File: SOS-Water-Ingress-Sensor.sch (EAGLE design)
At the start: 12 parts

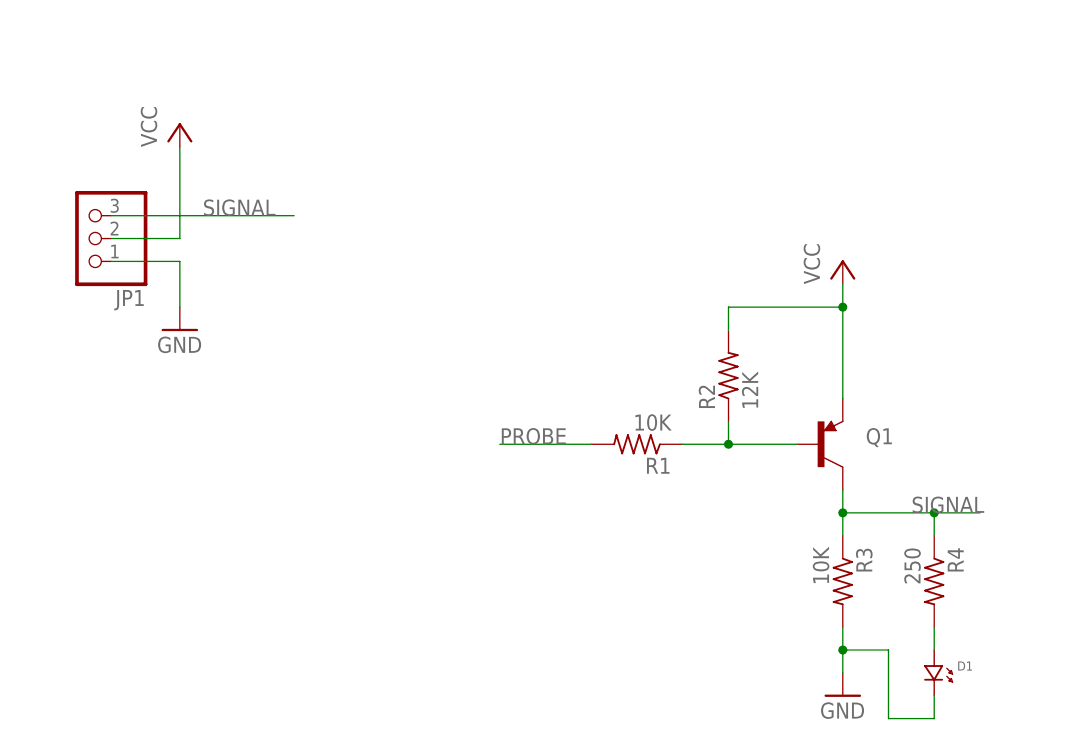
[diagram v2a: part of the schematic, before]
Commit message: Update silkscreen and layout.
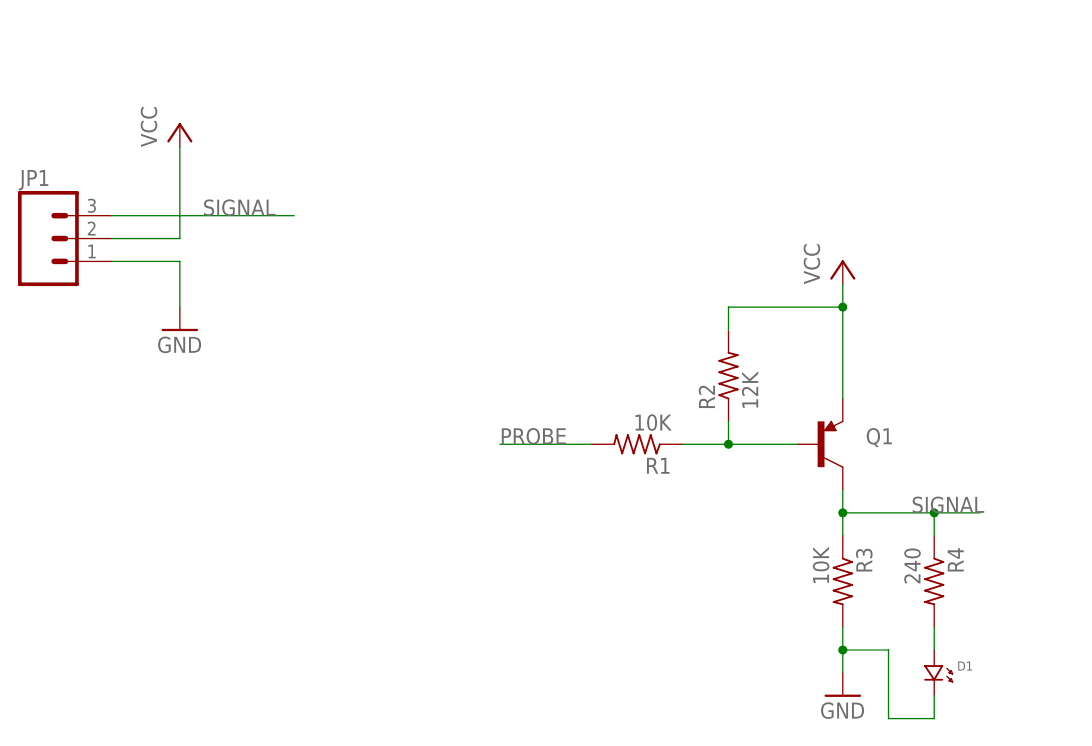
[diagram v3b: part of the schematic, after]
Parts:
- JP1: device pinhead+:PINHD-1X3 -> SparkFun-Connectors:M03PTH
- R4: value 250 -> 240
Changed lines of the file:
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@@
 <?xml version="1.0" encoding="utf-8"?>
 <!DOCTYPE eagle SYSTEM "eagle.dtd">
-<eagle version="7.6.0">
+<eagle version="7.4.0">
 <drawing>
 <settings>
@@
 <grid distance="0.1" unitdist="inch" unit="inch" style="lines" multiple="1" display="no" altdistance="0.01" altunitdist="inch" altunit="inch"/>
 <layers>
-<layer number="1" name="Top" color="4" fill="1" visible="no" active="no"/>
-<layer number="2" name="Route2" color="1" fill="3" visible="no" active="no"/>
-<layer number="3" name="Route3" color="4" fill="3" visible="no" active="no"/>
-<layer number="14" name="Route14" color="1" fill="6" visible="no" active="no"/>
-<layer number="15" name="Route15" color="4" fill="6" visible="no" active="no"/>
-<layer number="16" name="Bottom" color="1" fill="1" visible="no" active="no"/>
-<layer number="17" name="Pads" color="2" fill="1" visible="no" active="no"/>
-<layer number="18" name="Vias" color="2" fill="1" visible="no" active="no"/>
-<layer number="19" name="Unrouted" color="6" fill="1" visible="no" active="no"/>
-<layer number="20" name="Dimension" color="15" fill="1" visible="no" active="no"/>
-<layer number="21" name="tPlace" color="7" fill="1" visible="no" active="no"/>
-<layer number="22" name="bPlace" color="7" fill="1" visible="no" active="no"/>
-<layer number="23" name="tOrigins" color="15" fill="1" visible="no" active="no"/>
-<layer number="24" name="bOrigins" color="15" fill="1" visible="no" active="no"/>
-<layer number="25" name="tNames" color="7" fill="1" visible="no" active="no"/>
-<layer number="26" name="bNames" color="7" fill="1" visible="no" active="no"/>
-<layer number="27" name="tValues" color="7" fill="1" visible="no" active="no"/>
-<layer number="28" name="bValues" color="7" fill="1" visible="no" active="no"/>
+<layer number="1" name="Top" color="4" fill="1" visible="yes" active="no"/>
+<layer number="2" name="Route2" color="1" fill="3" visible="yes" active="no"/>
+<layer number="3" name="Route3" color="4" fill="3" visible="yes" active="no"/>
+<layer number="14" name="Route14" color="1" fill="6" visible="yes" active="no"/>
+<layer number="15" name="Route15" color="4" fill="6" visible="yes" active="no"/>
+<layer number="16" name="Bottom" color="1" fill="1" visible="yes" active="no"/>
+<layer number="17" name="Pads" color="2" fill="1" visible="yes" active="no"/>
+<layer number="18" name="Vias" color="2" fill="1" visible="yes" active="no"/>
+<layer number="19" name="Unrouted" color="6" fill="1" visible="yes" active="no"/>
+<layer number="20" name="Dimension" color="15" fill="1" visible="yes" active="no"/>
+<layer number="21" name="tPlace" color="7" fill="1" visible="yes" active="no"/>
+<layer number="22" name="bPlace" color="7" fill="1" visible="yes" active="no"/>
+<layer number="23" name="tOrigins" color="15" fill="1" visible="yes" active="no"/>
+<layer number="24" name="bOrigins" color="15" fill="1" visible="yes" active="no"/>
+<layer number="25" name="tNames" color="7" fill="1" visible="yes" active="no"/>
+<layer number="26" name="bNames" color="7" fill="1" visible="yes" active="no"/>
+<layer number="27" name="tValues" color="7" fill="1" visible="yes" active="no"/>
+<layer number="28" name="bValues" color="7" fill="1" visible="yes" active="no"/>
 <layer number="29" name="tStop" color="7" fill="3" visible="no" active="no"/>
 <layer number="30" name="bStop" color="7" fill="6" visible="no" active="no"/>
@@
 <layer number="35" name="tGlue" color="7" fill="4" visible="no" active="no"/>
 <layer number="36" name="bGlue" color="7" fill="5" visible="no" active="no"/>
-<layer number="37" name="tTest" color="7" fill="1" visible="no" active="no"/>
-<layer number="38" name="bTest" color="7" fill="1" visible="no" active="no"/>
+<layer number="37" name="tTest" color="7" fill="1" visible="yes" active="no"/>
+<layer number="38" name="bTest" color="7" fill="1" visible="yes" active="no"/>
 <layer number="39" name="tKeepout" color="4" fill="11" visible="no" active="no"/>
 <layer number="40" name="bKeepout" color="1" fill="11" visible="no" active="no"/>
@@
 <layer number="44" name="Drills" color="7" fill="1" visible="no" active="no"/>
 <layer number="45" name="Holes" color="7" fill="1" visible="no" active="no"/>
-<layer number="46" name="Milling" color="3" fill="1" visible="no" active="no"/>
-<layer number="47" name="Measures" color="7" fill="1" visible="no" active="no"/>
-<layer number="48" name="Document" color="7" fill="1" visible="no" active="no"/>
-<layer number="49" name="Reference" color="7" fill="1" visible="no" active="no"/>
-<layer number="50" name="dxf" color="7" fill="1" visible="no" active="no"/>
-<layer number="51" name="tDocu" color="7" fill="1" visible="no" active="no"/>
-<layer number="52" name="bDocu" color="7" fill="1" visible="no" active="no"/>
-<layer number="53" name="tGND_GNDA" color="7" fill="9" visible="no" active="no"/>
-<layer number="54" name="bGND_GNDA" color="1" fill="9" visible="no" active="no"/>
-<layer number="56" name="wert" color="7" fill="1" visible="no" active="no"/>
-<layer number="57" name="tCAD" color="7" fill="1" visible="no" active="no"/>
-<layer number="59" name="tCarbon" color="7" fill="1" visible="no" active="no"/>
-<layer number="60" name="bCarbon" color="7" fill="1" visible="no" active="no"/>
+<layer number="46" name="Milling" color="3" fill="1" visible="yes" active="no"/>
+<layer number="47" name="Measures" color="7" fill="1" visible="yes" active="no"/>
+<layer number="48" name="Document" color="7" fill="1" visible="yes" active="no"/>
+<layer number="49" name="Reference" color="7" fill="1" visible="yes" active="no"/>
+<layer number="50" name="dxf" color="7" fill="1" visible="yes" active="no"/>
+<layer number="51" name="tDocu" color="7" fill="1" visible="yes" active="no"/>
+<layer number="52" name="bDocu" color="7" fill="1" visible="yes" active="no"/>
+<layer number="53" name="tGND_GNDA" color="7" fill="9" visible="yes" active="no"/>
+<layer number="54" name="bGND_GNDA" color="1" fill="9" visible="yes" active="no"/>
+<layer number="56" name="wert" color="7" fill="1" visible="yes" active="no"/>
+<layer number="57" name="tCAD" color="7" fill="1" visible="yes" active="no"/>
+<layer number="59" name="tCarbon" color="7" fill="1" visible="yes" active="no"/>
+<layer number="60" name="bCarbon" color="7" fill="1" visible="yes" active="no"/>
 <layer number="90" name="Modules" color="5" fill="1" visible="yes" active="yes"/>
 <layer number="91" name="Nets" color="2" fill="1" visible="yes" active="yes"/>
@@
 <part name="U$2" library="BlueRobotics-JST-GH" deviceset="JSH-GH-2" device="VERT"/>
 <part name="U$3" library="BlueRobotics-JST-GH" deviceset="JSH-GH-2" device="VERT"/>
-<part name="JP1" library="pinhead+" deviceset="PINHD-1X3" device=""/>
-<part name="R4" library="resistor" deviceset="R-US_" device="R0603" value="250"/>
+<part name="R4" library="resistor" deviceset="R-US_" device="R0603" value="240"/>
 <part name="D1" library="standardparts" deviceset="LED" device=".0805"/>
 <part name="U$4" library="BlueRobotics-JST-GH" deviceset="JSH-GH-2" device="VERT"/>
+<part name="JP1" library="SparkFun-Connectors" deviceset="M03" device="PTH"/>
 </parts>
 <sheets>
@@
 <instance part="U$2" gate="G$1" x="187.96" y="114.3"/>
 <instance part="U$3" gate="G$1" x="187.96" y="101.6"/>
-<instance part="JP1" gate="A" x="48.26" y="127" rot="R180"/>
 <instance part="R4" gate="G$1" x="142.24" y="88.9" rot="R270"/>
 <instance part="D1" gate="G$1" x="142.24" y="78.74" rot="R270"/>
 <instance part="U$4" gate="G$1" x="187.96" y="88.9"/>
+<instance part="JP1" gate="G$1" x="43.18" y="127"/>
 </instances>
 <busses>
@@
 <wire x1="58.42" y1="127" x2="58.42" y2="137.16" width="0.1524" layer="91"/>
 <wire x1="50.8" y1="127" x2="58.42" y2="127" width="0.1524" layer="91"/>
-<pinref part="JP1" gate="A" pin="2"/>
+<pinref part="JP1" gate="G$1" pin="2"/>
 </segment>
 <segment>
@@
 <wire x1="50.8" y1="124.46" x2="58.42" y2="124.46" width="0.1524" layer="91"/>
 <wire x1="58.42" y1="124.46" x2="58.42" y2="119.38" width="0.1524" layer="91"/>
-<pinref part="JP1" gate="A" pin="1"/>
+<pinref part="JP1" gate="G$1" pin="1"/>
 </segment>
 <segment>
@@
 <wire x1="50.8" y1="129.54" x2="71.12" y2="129.54" width="0.1524" layer="91"/>
 <label x="60.96" y="129.54" size="1.778" layer="95"/>
-<pinref part="JP1" gate="A" pin="3"/>
-</segment>
-<segment>
+<pinref part="JP1" gate="G$1" pin="3"/>
+</segment>
+<segment>

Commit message: Minor tweaks to layout all around.
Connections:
- net GND: now also U$1.G, U$2.G, U$3.G, U$4.G
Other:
- moved on the sheet: D1, JP1, Q1, R1, R2, R3, R4
